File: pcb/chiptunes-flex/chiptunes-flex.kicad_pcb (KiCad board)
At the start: 2 copper layers, 21.9 x 9.7 mm, 7 parts, among them U1 ATtiny4

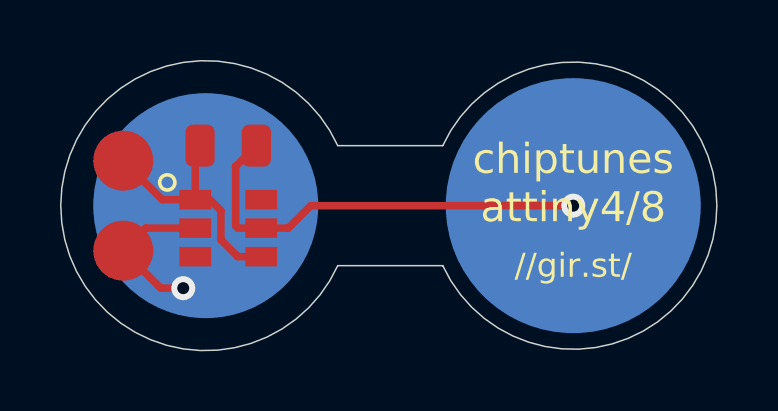
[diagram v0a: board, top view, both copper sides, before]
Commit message: pcb: add low pass filter
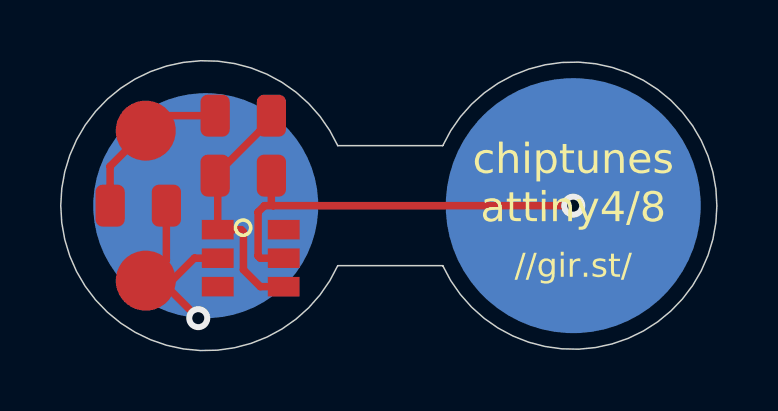
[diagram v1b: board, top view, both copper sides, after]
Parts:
- removed REF**: TestPoint_Pad_2.5x2.5mm, TestPoint:TestPoint_Pad_2.5x2.5mm
- added C1: 100n, Capacitor_SMD:C_0805_2012Metric, F.Cu at (147.8, 95.0)
- added R2: 200, Resistor_SMD:R_0805_2012Metric, F.Cu at (151.2, 92.0)
- U1: value ATtiny4 -> ATtiny4-TS
- moved TP3 1.25 mm to (148.0, 92.5)
- moved TP4 1.25 mm to (148.0, 97.5)
- moved U1 1.25 mm to (151.5, 96.8)
- moved R1 1.12 mm to (151.2, 94.0)
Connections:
- TP3 pad 1: Net-(R1-Pad2) -> Net-(C1-Pad1)
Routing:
- net Net-(C1-Pad1): track 0.00 -> 5.51 mm
- net GND: track 12.2 -> 15.5 mm
- net +3V0: track 14.6 -> 14.0 mm
